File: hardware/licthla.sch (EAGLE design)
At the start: 8 parts, among them U1 NCP1117LPST50T3G

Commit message: Some more work on the AVR part of the schematic
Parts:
- added C4, C5, C6: .1uF, MF_Passives:CAPACITOR_NP_0402
- added D3, D4, D5: amber, MF_LEDs:LED_SINGLE_0805
- added J2, J3: (no value), MF_Connectors:HEADER_01X15_PTH_2.54MM
- added J4: (no value), MF_Connectors:USB_MICRO_RIGHT
- added R2, R3: 1K, MF_Passives:RESISTOR_0805
- added R4, R5, R6, R7: 470, MF_Passives:RESISTOR_0805
- added SW1: (no value), MF_Switches:TACT_6MM
- added U$1: 16Mhz, adafruit:CERMOSCILL-AWCSR
- added U2: ATMEGA328P-AU, MF_IC_Digital:ATMEGA328P-AU
- added U3: FT232RL, MF_IC_Digital:FT232RL
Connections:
- new net +3V3: C6.P$2, J3.PIN13, U3.3V3OUT
- new net A0: J3.PIN11, U2.PC0
- new net A1: J3.PIN10, U2.PC1
- new net A2: J3.PIN9, U2.PC2
- new net A3: J3.PIN8, U2.PC3
- new net A4: J3.PIN7, U2.PC4
- new net A5: J3.PIN6, U2.PC5
- new net A6: J3.PIN5, U2.ADC6
- new net A7: J3.PIN4, U2.ADC7
- new net AREF: C4.P$1, J3.PIN12, U2.AREF
- new net D0: J2.PIN1, R2.P$1, U2.PD0
- new net D1: J2.PIN0, R3.P$2, U2.PD1
- new net D10: J2.PIN12, U2.PB2
- new net D11: J2.PIN13, U2.PB3
- new net D12: J2.PIN14, U2.PB4
- new net D13: J3.PIN14, R4.P$1, U2.PB5
- new net D2: J2.PIN4, U2.PD2
- new net D3: J2.PIN5, U2.PD3
- new net D4: J2.PIN6, U2.PD4
- new net D5: J2.PIN7, U2.PD5
- new net D6: J2.PIN8, U2.PD6
- new net D7: J2.PIN9, U2.PD7
- new net D8: J2.PIN10, U2.PB0
- new net D9: J2.PIN11, U2.PB1
- new net N$11: D4.CATHODE, R6.P$1
- new net N$12: D5.CATHODE, R7.P$1
- new net N$13: R6.P$2, U3.CBUS0
- new net N$14: R7.P$2, U3.CBUS1
- new net N$2: J4.D-, U3.USBDM
- new net N$5: U$1.IN, U2.PB7
- new net N$6: U$1.OUT, U2.PB6
- new net N$7: D3.ANODE, R4.P$2
- new net N$8: C5.P$2, U3.!RESET
- new net RESET: C5.P$1, J2.PIN2, J3.PIN2, R5.P$2, U2.PC6
- new net RX: R2.P$2, U3.TXD
- new net TX: R3.P$1, U3.RXD
- new net V+: D1.ANODE, J1.PIN0, J3.PIN0
- new net VUSB: J4.5V
- net +5V: now also D4.ANODE, D5.ANODE, J3.PIN3, R5.P$1, U2.AVCC, U2.VCC, U3.VCC, U3.VCCIO
- net GND: now also C4.P$2, C6.P$1, D3.CATHODE, J2.PIN3, J3.PIN1, J4.GND, J4.SLD, U$1.GND, U2.GND, U3.AGND, U3.GND
- net N$3: now also J4.D+, U3.USBDP; no longer D1.ANODE, J1.PIN0
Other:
- note added: "AVR controller"
- note added: "Power Supply"
- note added: "USB"
- moved on the sheet: C1, C2, C3, D1, D2, J1, R1, U1

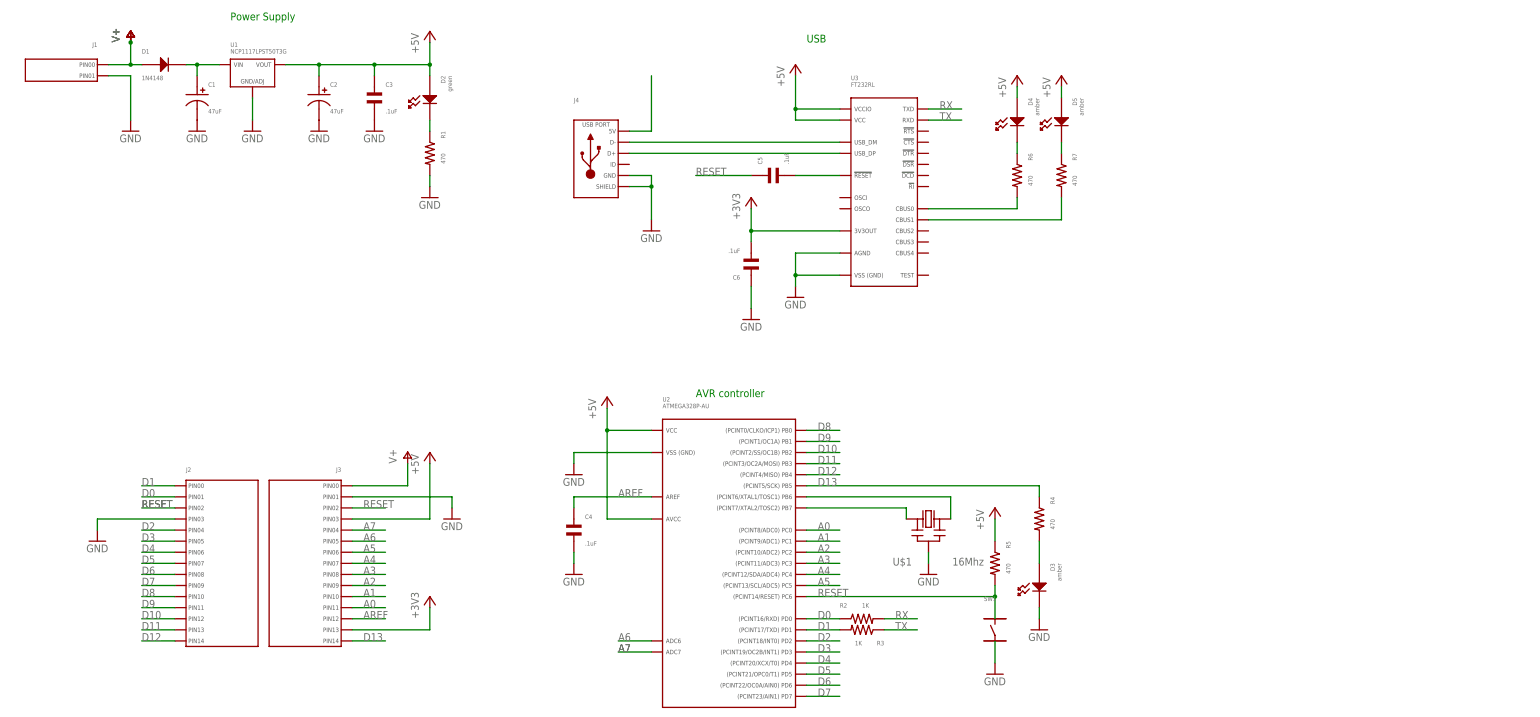
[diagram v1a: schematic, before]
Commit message: Added LED PWM driver
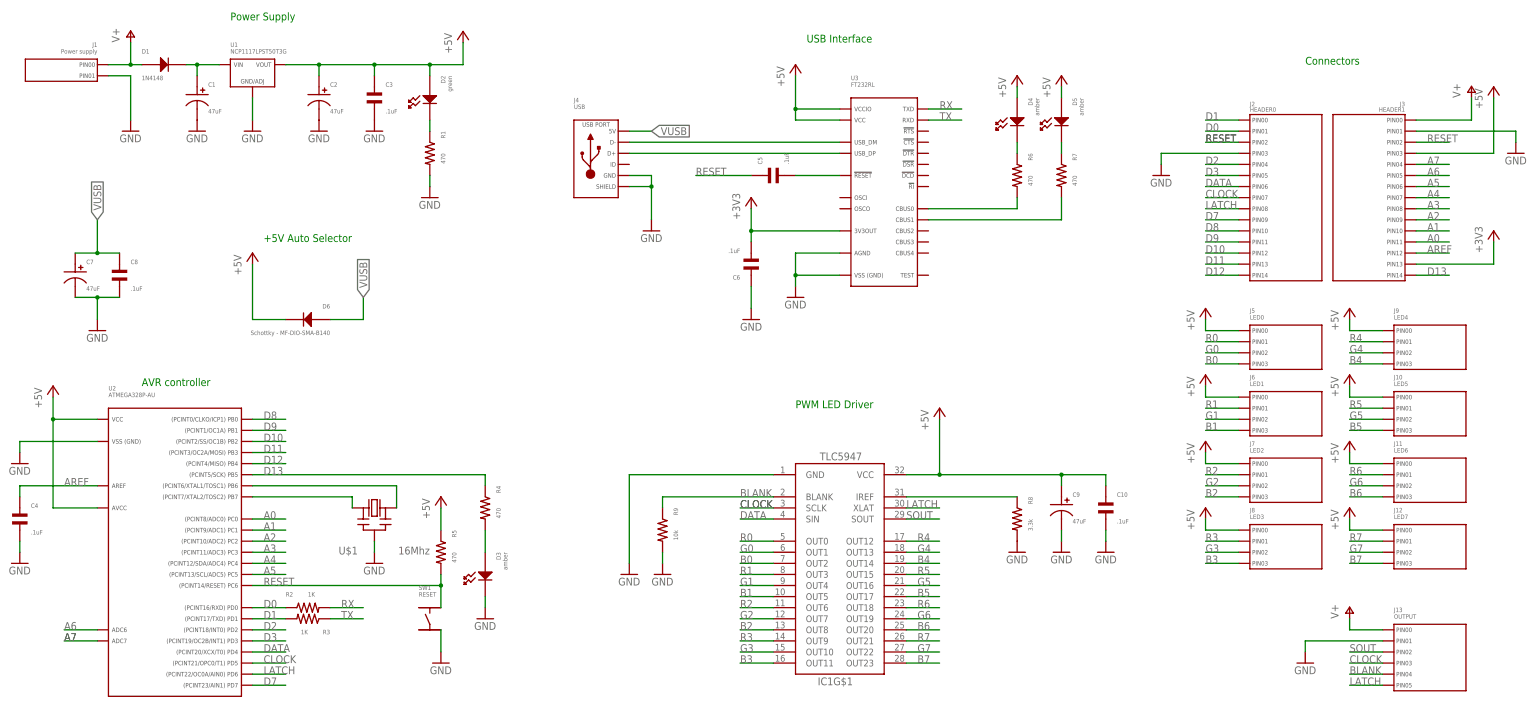
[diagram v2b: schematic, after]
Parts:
- added C10, C8: .1uF, MF_Passives:CAPACITOR_NP_0402
- added C7, C9: 47uF, MF_Passives:CAPACITOR_P_6.3MM
- added D6: Schottky - MF-DIO-SMA-B140, MF_Discrete_Semiconductor:DIODE_SMA
- added IC1: TLC5947-DAP, adafruit:TLC5947-DAP
- added J10: LED5, MF_Connectors:HEADER_01X04_PTH_2.54MM
- added J11: LED6, MF_Connectors:HEADER_01X04_PTH_2.54MM
- added J12: LED7, MF_Connectors:HEADER_01X04_PTH_2.54MM
- added J13: OUTPUT, MF_Connectors:HEADER_01X06_PTH_2.54MM
- added J5: LED0, MF_Connectors:HEADER_01X04_PTH_2.54MM
- added J6: LED1, MF_Connectors:HEADER_01X04_PTH_2.54MM
- added J7: LED2, MF_Connectors:HEADER_01X04_PTH_2.54MM
- added J8: LED3, MF_Connectors:HEADER_01X04_PTH_2.54MM
- added J9: LED4, MF_Connectors:HEADER_01X04_PTH_2.54MM
- added R8: 3.3k, MF_Passives:RESISTOR_0805
- added R9: 10k, MF_Passives:RESISTOR_0805
- J1: value (none) -> Power supply
- J2: value (none) -> HEADER0
- J3: value (none) -> HEADER1
- J4: value (none) -> USB
- SW1: value (none) -> RESET
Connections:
- removed net D4: J2.PIN6, U2.PD4
- removed net D5: J2.PIN7, U2.PD5
- removed net D6: J2.PIN8, U2.PD6
- new net B0: IC1G$1.OUT2, J5.PIN3
- new net B1: IC1G$1.OUT5, J6.PIN3
- new net B2: IC1G$1.OUT8, J7.PIN3
- new net B3: IC1G$1.OUT11, J8.PIN3
- new net B4: IC1G$1.OUT14, J9.PIN3
- new net B5: IC1G$1.OUT17, J10.PIN3
- new net B6: IC1G$1.OUT20, J11.PIN3
- new net B7: IC1G$1.OUT23, J12.PIN3
- new net BLANK: IC1G$1.BLANK, J13.PIN4, R9.P$1
- new net CLOCK: IC1G$1.SCLK, J13.PIN3, J2.PIN7, U2.PD5
- new net DATA: IC1G$1.SIN, J2.PIN6, U2.PD4
- new net G0: IC1G$1.OUT1, J5.PIN2
- new net G1: IC1G$1.OUT4, J6.PIN2
- new net G2: IC1G$1.OUT7, J7.PIN2
- new net G3: IC1G$1.OUT10, J8.PIN2
- new net G4: IC1G$1.OUT13, J9.PIN2
- new net G5: IC1G$1.OUT16, J10.PIN2
- new net G6: IC1G$1.OUT19, J11.PIN2
- new net G7: IC1G$1.OUT22, J12.PIN2
- new net LATCH: IC1G$1.XLAT, J13.PIN5, J2.PIN8, U2.PD6
- new net N$9: IC1G$1.IREF, R8.P$1
- new net R0: IC1G$1.OUT0, J5.PIN1
- new net R1: IC1G$1.OUT3, J6.PIN1
- new net R2: IC1G$1.OUT6, J7.PIN1
- new net R3: IC1G$1.OUT9, J8.PIN1
- new net R4: IC1G$1.OUT12, J9.PIN1
- new net R5: IC1G$1.OUT15, J10.PIN1
- new net R6: IC1G$1.OUT18, J11.PIN1
- new net R7: IC1G$1.OUT21, J12.PIN1
- new net SOUT: IC1G$1.SOUT, J13.PIN2
- net +5V: now also C10.P$1, C9.P$1, D6.CATHODE, IC1G$1.VCC, J10.PIN0, J11.PIN0, J12.PIN0, J5.PIN0, J6.PIN0, J7.PIN0, J8.PIN0, J9.PIN0
- net GND: now also C10.P$2, C7.P$2, C8.P$2, C9.P$2, IC1G$1.GND, J13.PIN1, R8.P$2, R9.P$2, SW1.P$4
- net RESET: now also SW1.P$2
- net V+: now also J13.PIN0
- net VUSB: now also C7.P$1, C8.P$1, D6.ANODE
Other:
- note added: "+5V Auto Selector"
- note added: "Connectors"
- note added: "PWM LED Driver"
- note added: "USB Interface"
- note removed: "USB"
- moved on the sheet: C4, D3, J2, J3, R2, R3, R4, R5, SW1, U$1, U2

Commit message: Start to add the provision for a BLE shield - This will still change as I currently tend for the Adafruit one
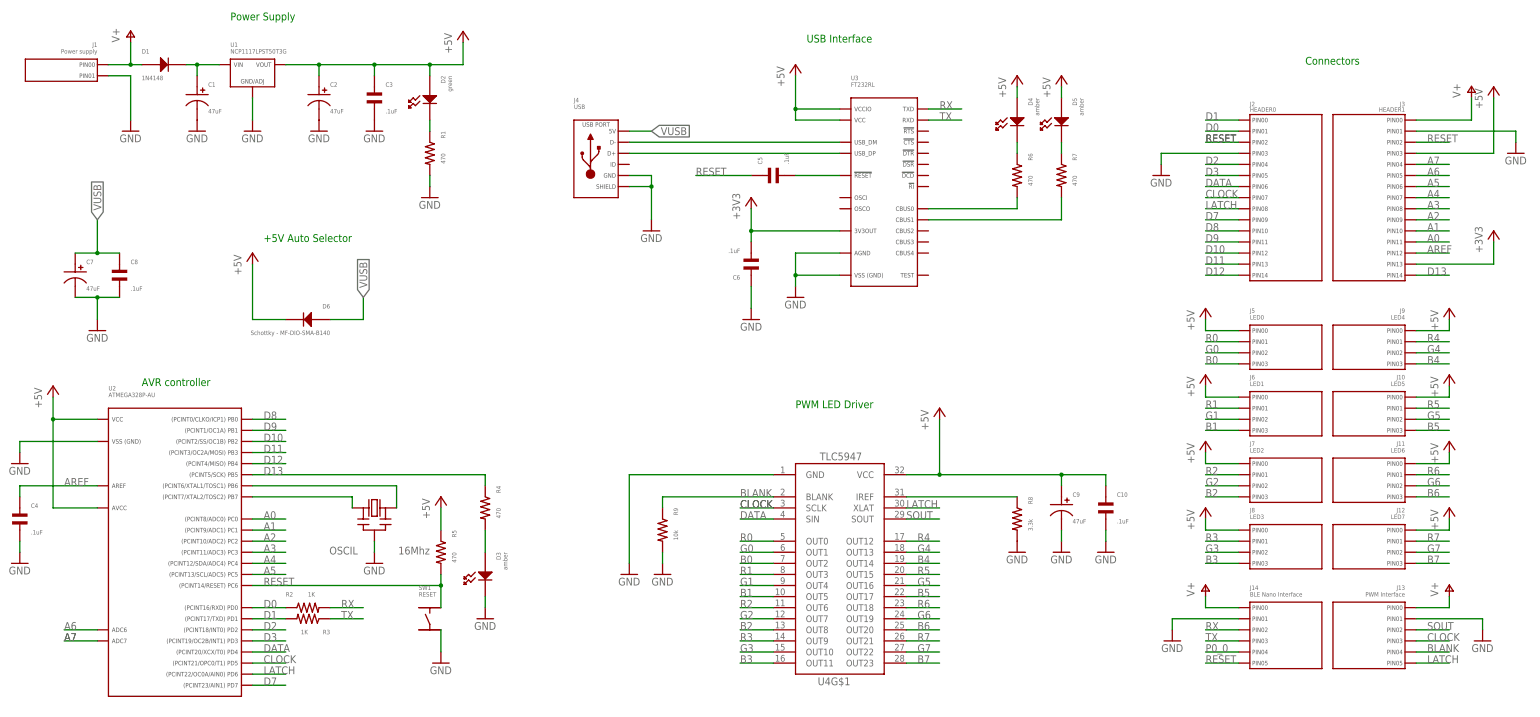
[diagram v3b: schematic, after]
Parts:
- added J14: BLE Nano Interface, MF_Connectors:HEADER_01X06_PTH_2.54MM
- J13: value OUTPUT -> PWM Interface
- renumbered IC1 to U4, U$1 to OSCIL
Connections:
- new net P0_0: J14.PIN4
- net GND: now also J14.PIN1
- net RESET: now also J14.PIN5
- net RX: now also J14.PIN2
- net TX: now also J14.PIN3
- net V+: now also J14.PIN0
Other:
- moved on the sheet: J10, J11, J12, J13, J9
